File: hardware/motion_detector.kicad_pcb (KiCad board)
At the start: 2 copper layers, 45 x 25 mm, 36 parts, among them J1 Debug, P1 CON-SENSOR2, P2 Boot, U1 XMC1XXX24, U2 MCP4018, U3 AM612, U4 DRILL, U5 DRILL, U6 DRILL, U7 DRILL

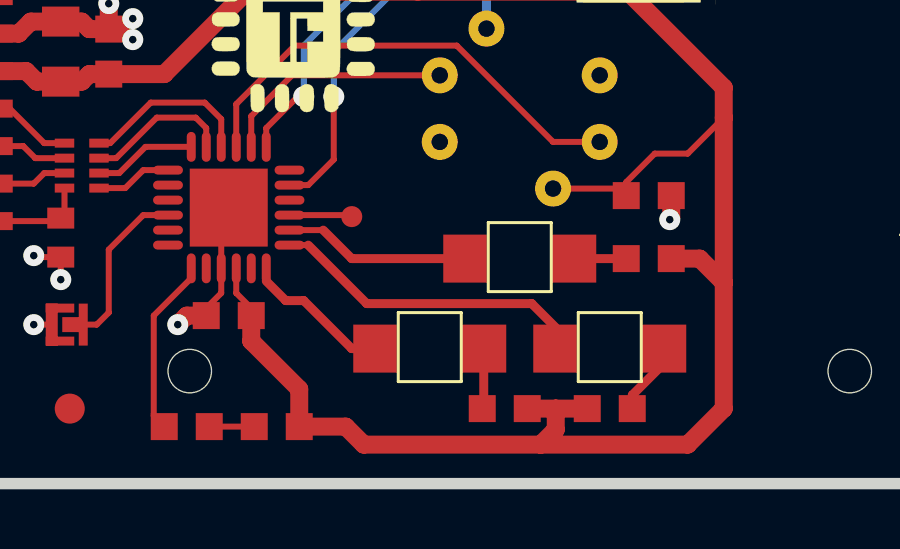
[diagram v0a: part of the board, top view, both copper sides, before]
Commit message: add cutouts for leds
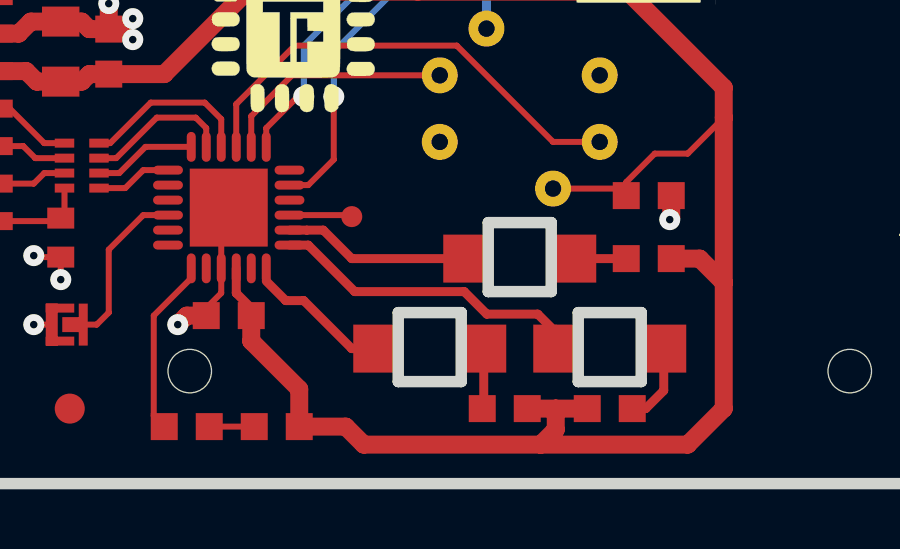
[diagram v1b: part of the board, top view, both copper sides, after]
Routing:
- net Net-(D3-Pad1): track 2.43 -> 3.20 mm
- net LED_GREEN: track 10.7 -> 11.3 mm
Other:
- outline, holes or cut-outs redrawn
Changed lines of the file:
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@@
     (area 42.044999 28.944999 282.27147 165.489573)
     (thickness 1.6002)
-    (drawings 13)
-    (tracks 211)
+    (drawings 25)
+    (tracks 216)
     (zones 0)
     (modules 36)
@@
   )
   (layers
-    (0 Vorderseite jumper hide)
+    (0 Vorderseite jumper)
     (31 Rückseite jumper hide)
     (32 B.Adhes user)
@@
     (34 B.Paste user)
     (35 F.Paste user)
-    (36 B.SilkS user)
-    (37 F.SilkS user hide)
+    (36 B.SilkS user hide)
+    (37 F.SilkS user)
     (38 B.Mask user)
     (39 F.Mask user)
@@
     (aux_axis_origin 42.9 54.8)
     (grid_origin 42.9 54.8)
-    (visible_elements FFFFBFBF)
+    (visible_elements FFFFDFBF)
     (pcbplotparams
       (layerselection 0x00030_80000001)
@@
       (xy 3.1242 -3.1242)) (layer B.SilkS) (width 0.00254))
   )
+  (gr_line (start 69.45 49.1) (end 67.35 49.1) (angle 90) (layer Edge.Cuts) (width 0.381))
+  (gr_line (start 69.45 51.4) (end 69.45 49.1) (angle 90) (layer Edge.Cuts) (width 0.381))
+  (gr_line (start 67.35 51.4) (end 69.45 51.4) (angle 90) (layer Edge.Cuts) (width 0.381))
+  (gr_line (start 67.35 49.1) (end 67.35 51.4) (angle 90) (layer Edge.Cuts) (width 0.381))
+  (gr_line (start 63.45 49.1) (end 61.35 49.1) (angle 90) (layer Edge.Cuts) (width 0.381))
+  (gr_line (start 63.45 51.4) (end 63.45 49.1) (angle 90) (layer Edge.Cuts) (width 0.381))
+  (gr_line (start 61.35 51.4) (end 63.45 51.4) (angle 90) (layer Edge.Cuts) (width 0.381))
+  (gr_line (start 61.35 49.1) (end 61.35 51.4) (angle 90) (layer Edge.Cuts) (width 0.381))
+  (gr_line (start 64.35 48.4) (end 64.35 46.1) (angle 90) (layer Edge.Cuts) (width 0.381))
+  (gr_line (start 66.45 48.4) (end 64.35 48.4) (angle 90) (layer Edge.Cuts) (width 0.381))
+  (gr_line (start 66.45 46.1) (end 66.45 48.4) (angle 90) (layer Edge.Cuts) (width 0.381))
+  (gr_line (start 64.35 46.1) (end 66.45 46.1) (angle 90) (layer Edge.Cuts) (width 0.381))
   (gr_text "Motion\nDetector\n2.0" (at 48.2 42.3) (layer B.SilkS)
     (effects (font (size 0.8 0.8) (thickness 0.15)) (justify mirror))
@@
   (segment (start 63.45 33.15) (end 63.45 31.7) (width 0.29972) (layer Vorderseite) (net 2))
   (segment (start 63.45 31.7) (end 63.55 31.6) (width 0.2) (layer Vorderseite) (net 2))
-  (segment (start 55.95 47.625) (end 55.95 48.45) (width 0.2) (layer Vorderseite) (net 2))
-  (segment (start 55.95 48.45) (end 56.45 48.95) (width 0.2) (layer Vorderseite) (net 2))
+  (segment (start 55.95 47.625) (end 55.95 48.45) (width 0.29972) (layer Vorderseite) (net 2))
+  (segment (start 55.95 48.45) (end 56.45 48.95) (width 0.29972) (layer Vorderseite) (net 2))
   (segment (start 56.45 48.95) (end 56.45 49.2) (width 0.2) (layer Vorderseite) (net 2))
   (segment (start 50.225 44.9493) (end 50.225 45.825) (width 0.2) (layer Vorderseite) (net 3))
@@
   (segment (start 55.05 52.9) (end 56.55 52.9) (width 0.2) (layer Vorderseite) (net 5))
   (segment (start 67.2 47.3) (end 68.95 47.3) (width 0.29972) (layer Vorderseite) (net 6))
-  (segment (start 57.725 46.35) (end 58.85 46.35) (width 0.2) (layer Vorderseite) (net 7))
-  (segment (start 59.8 47.3) (end 63.6 47.3) (width 0.29972) (layer Vorderseite) (net 7))
+  (segment (start 58.3 46.35) (end 57.725 46.35) (width 0.29972) (layer Vorderseite) (net 7))
   (segment (start 58.85 46.35) (end 59.8 47.3) (width 0.29972) (layer Vorderseite) (net 7))
+  (segment (start 59.8 47.3) (end 63.6 47.3) (width 0.29972) (layer Vorderseite) (net 7))
+  (segment (start 58.85 46.35) (end 58.3 46.35) (width 0.29972) (layer Vorderseite) (net 7))
+  (segment (start 70.2 50.3) (end 70.2 51.7) (width 0.29972) (layer Vorderseite) (net 8))
+  (segment (start 70.2 51.7) (end 69.6 52.3) (width 0.29972) (layer Vorderseite) (net 8))
+  (segment (start 69.6 52.3) (end 69.15 52.3) (width 0.29972) (layer Vorderseite) (net 8))
   (segment (start 70.2 50.3) (end 70.2 50.8) (width 0.29972) (layer Vorderseite) (net 8))
-  (segment (start 70.2 50.8) (end 69.15 51.85) (width 0.29972) (layer Vorderseite) (net 8))
-  (segment (start 69.15 51.85) (end 69.15 52.3) (width 0.29972) (layer Vorderseite) (net 8))
-  (segment (start 57.725 46.85) (end 58.35 46.85) (width 0.2) (layer Vorderseite) (net 9))
-  (segment (start 65.8 48.8) (end 66.6 49.6) (width 0.29972) (layer Vorderseite) (net 9))
-  (segment (start 60.3 48.8) (end 65.8 48.8) (width 0.29972) (layer Vorderseite) (net 9))
-  (segment (start 58.35 46.85) (end 60.3 48.8) (width 0.29972) (layer Vorderseite) (net 9))
+  (segment (start 58.35 46.85) (end 57.725 46.85) (width 0.29972) (layer Vorderseite) (net 9))
+  (segment (start 66.6 50.3) (end 66.6 49.75) (width 0.29972) (layer Vorderseite) (net 9))
+  (segment (start 66.6 49.75) (end 66 49.15) (width 0.29972) (layer Vorderseite) (net 9))
+  (segment (start 59.9 48.4) (end 58.35 46.85) (width 0.29972) (layer Vorderseite) (net 9))
+  (segment (start 63.55 48.4) (end 59.9 48.4) (width 0.29972) (layer Vorderseite) (net 9))
+  (segment (start 64.3 49.15) (end 63.55 48.4) (width 0.29972) (layer Vorderseite) (net 9))
+  (segment (start 66 49.15) (end 64.3 49.15) (width 0.29972) (layer Vorderseite) (net 9))
   (segment (start 66.6 49.6) (end 66.6 50.3) (width 0.2) (layer Vorderseite) (net 9))
   (segment (start 64.2 50.3) (end 64.2 52.25) (width 0.29972) (layer Vorderseite) (net 10))

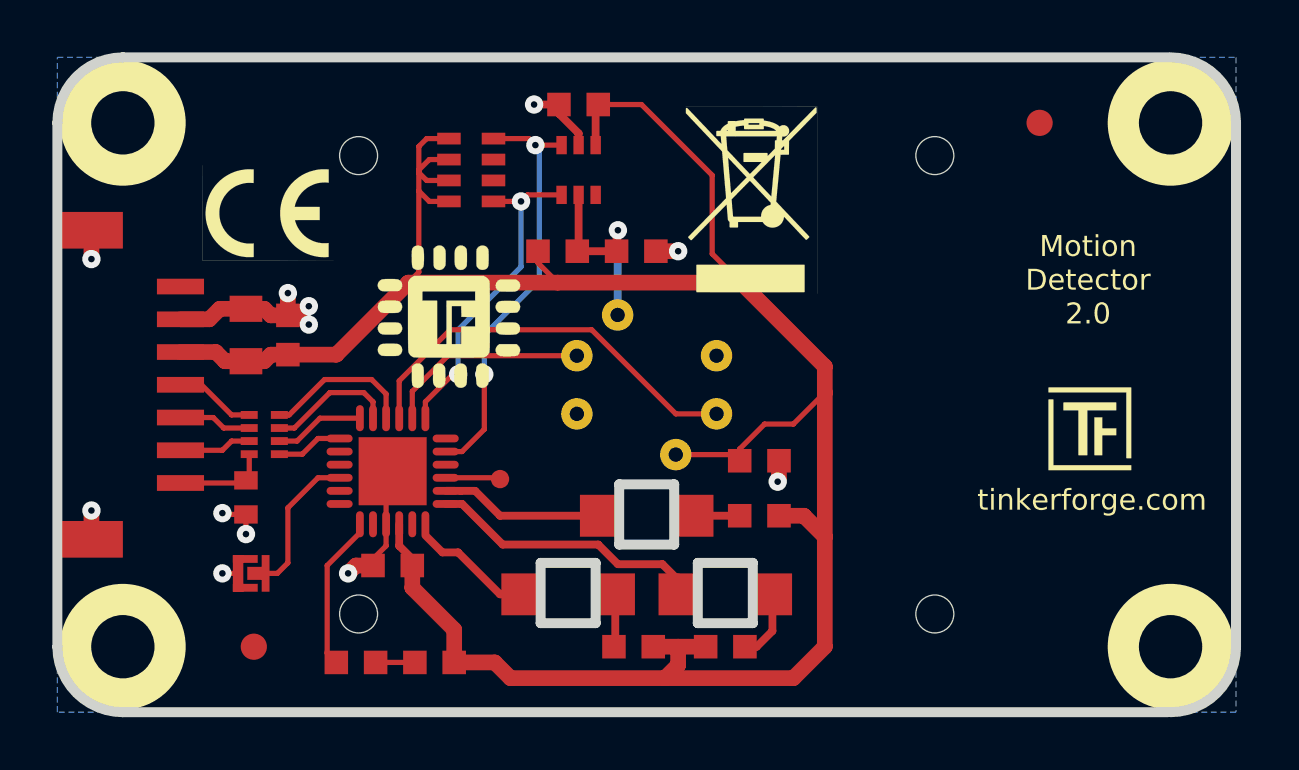
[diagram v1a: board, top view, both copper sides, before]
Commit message: fix ams612 routing, change led positions
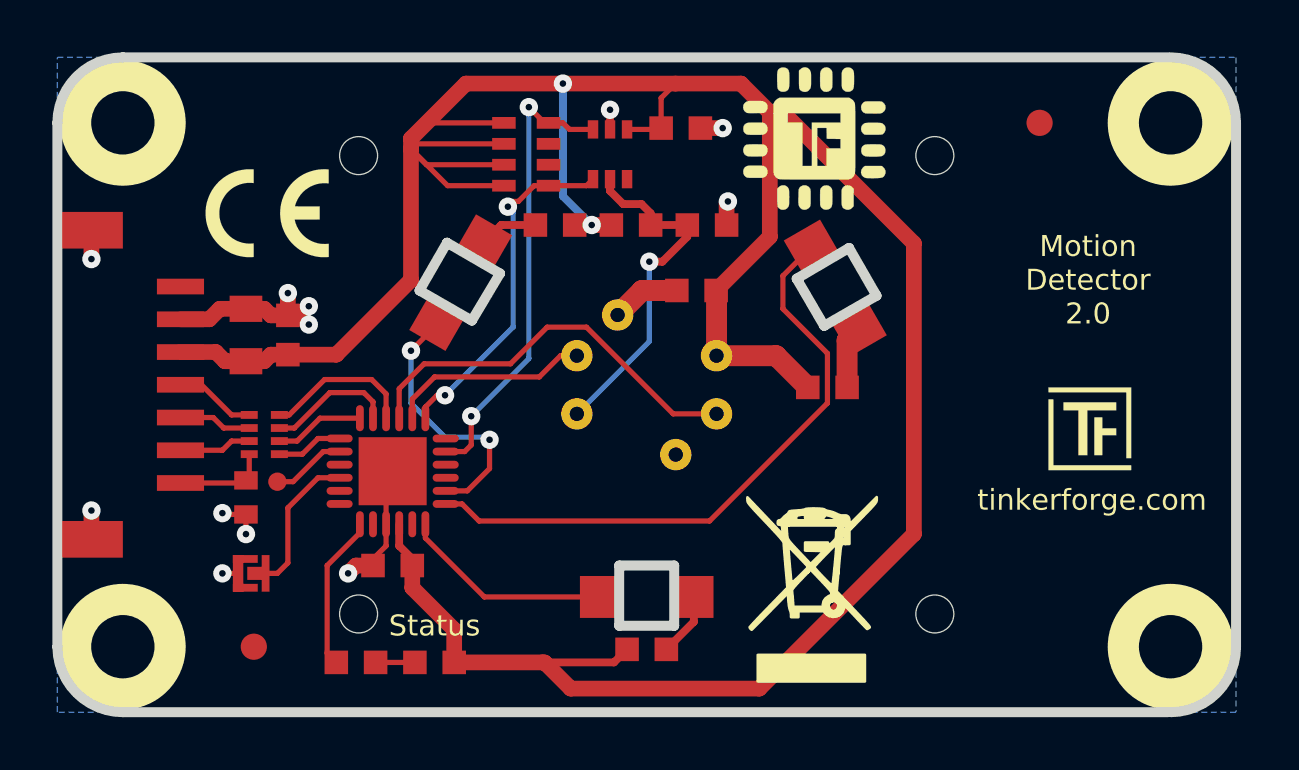
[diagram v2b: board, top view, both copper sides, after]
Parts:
- U4, U5, U6, U7: footprint kicad-libraries:DRILL_NP -> DRILL_NP
- VAL: footprint WEEE_7mm -> kicad-libraries:WEEE_7mm
- VAL: footprint CE_5mm -> kicad-libraries:CE_5mm
- moved G*** 15.5 mm to (71.8, 32.9)
- moved VAL 15.0 mm to (71.7, 50.1), turned to 0 degrees
- moved R3 13.6 mm to (61.9, 36.2)
- moved D3 12.4 mm to (72.6, 38.6), turned to 120 degrees
- moved D2 11.4 mm to (58.3, 38.4), turned to 240 degrees
- moved R4 10.6 mm to (72.3, 42.4)
- moved J1 8.50 mm to (51.3, 46.0)
- moved C7 6.93 mm to (67.3, 38.7), turned to 0 degrees
- moved C6 4.00 mm to (66.7, 32.5), turned to 180 degrees
- moved D4 3.00 mm to (65.4, 50.4)
- moved R2 2.97 mm to (64.8, 36.2)
- moved C5 2.88 mm to (67.7, 36.2)
- moved RP2 2.18 mm to (60.8, 33.5)
- moved U2 1.34 mm to (64.0, 33.5)
- moved R5 0.51 mm to (65.4, 52.4), turned to 180 degrees
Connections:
- U1 pad 15: Net-(J1-Pad1) -> (no net)
- U1 pad 2: (no net) -> Net-(J1-Pad1)
- U3 pad 1: GND -> VSENS
- U3 pad 3: VSENS -> GND
- U3 pad 4: GND -> VCC
- U3 pad 6: VCC -> GND
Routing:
- net VCC: track 95.4 -> 119.3 mm, vias 0 -> 2
- net LED_GREEN: track 11.3 -> 23.8 mm
- net VSENS: track 7.79 -> 13.7 mm
- net LED_RED: track 6.27 -> 10.2 mm, vias 0 -> 2
- net LED_BLUE: track 5.01 -> 8.53 mm
- net SCL: track 16.3 -> 17.7 mm
- net SDA: track 12.6 -> 13.4 mm
- net Net-(D3-Pad1): track 3.20 -> 2.43 mm
- net Net-(J1-Pad1): track 2.10 -> 2.85 mm
- net GND: track 25.6 -> 26.3 mm
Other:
- outline, holes or cut-outs redrawn
- board text added: "Status"

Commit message: version without i2c poti, uses rc circuit
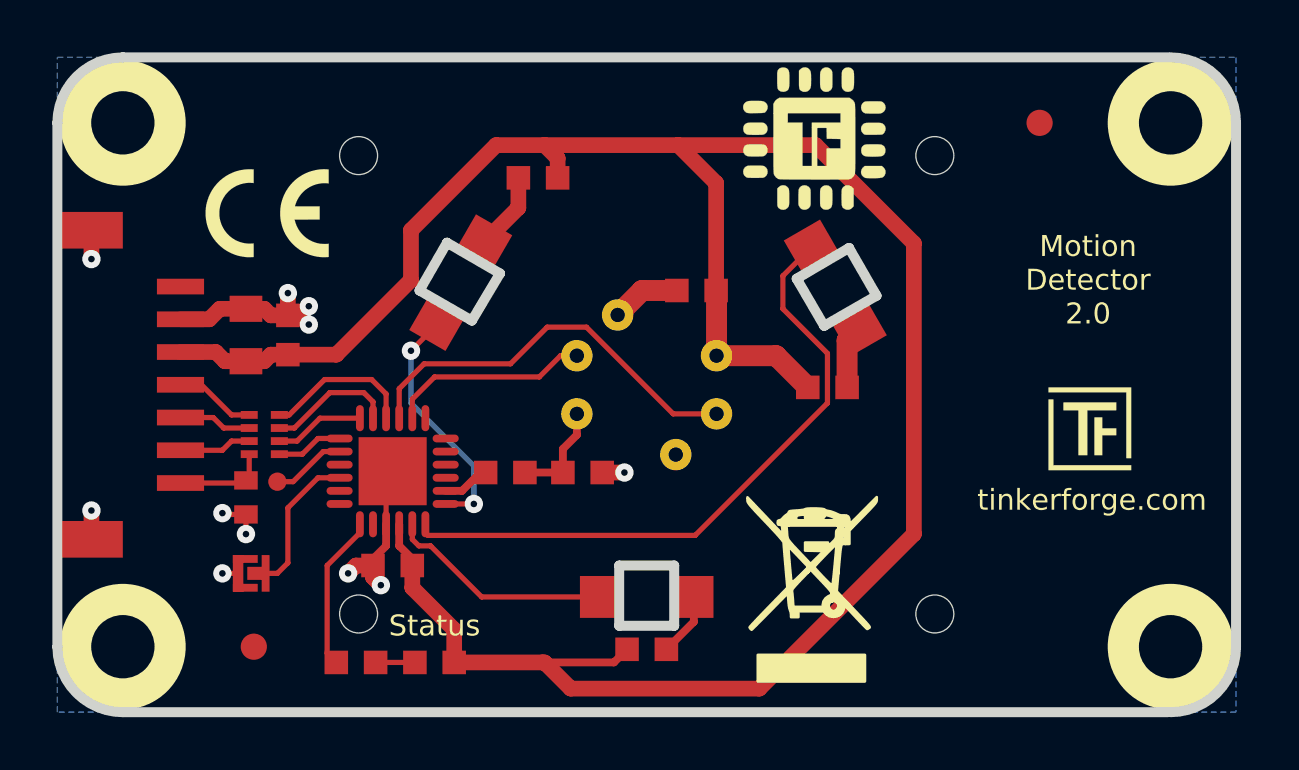
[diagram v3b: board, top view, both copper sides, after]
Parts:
- removed C5: 100nF, C0603F
- removed RP2: 4k7, kicad-libraries:4X0603
- removed U2: MCP4018, kicad-libraries:SC70-6
- R2: value 30k -> 1k
- moved C6 13.7 mm to (63.0, 45.6)
- moved R2 10.6 mm to (60.0, 45.6)
- moved R3 1.91 mm to (61.2, 34.4)
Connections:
- C6 pad 2: VCC -> VSENS
- R2 pad 1: VCC -> Net-(R2-Pad1)
- U1 pad 11: (no net) -> LED_BLUE
- U1 pad 12: LED_BLUE -> LED_GREEN
- U1 pad 13: LED_GREEN -> LED_RED
- U1 pad 14: LED_RED -> Net-(R2-Pad1)
- U1 pad 17: SCL -> (no net)
- U1 pad 19: SDA -> (no net)
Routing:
- net VCC: track 119.3 -> 89.4 mm, vias 2 -> 0
- net SCL: track 17.7 -> 0.00 mm, vias 2 -> 0
- net SDA: track 13.4 -> 0.00 mm, vias 2 -> 0
- net VSENS: track 13.7 -> 3.91 mm, vias 1 -> 0
- net Net-(R2-Pad1): track 0.00 -> 1.81 mm
- net LED_GREEN: track 23.8 -> 24.9 mm
- net GND: track 26.3 -> 25.5 mm, vias 12 -> 11
- net LED_RED: track 10.2 -> 9.37 mm
- net Net-(D2-Pad1): track 2.22 -> 2.98 mm

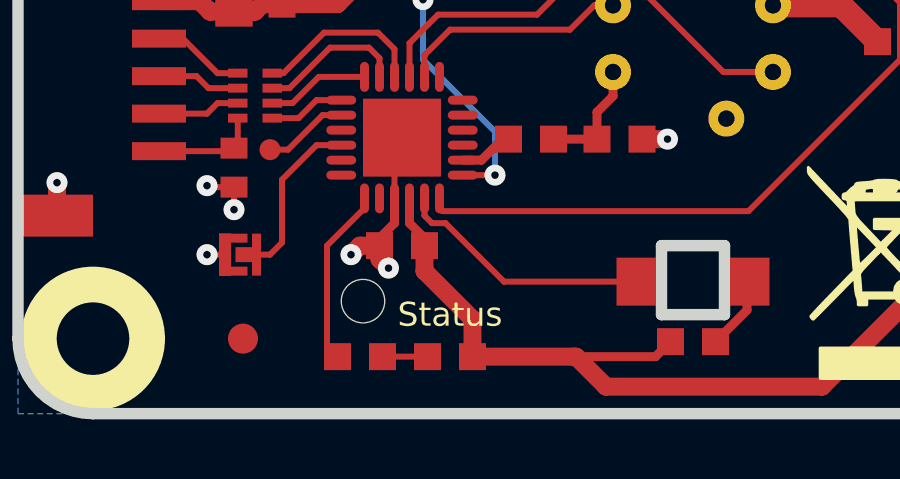
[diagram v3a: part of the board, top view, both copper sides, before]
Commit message: fix status led text
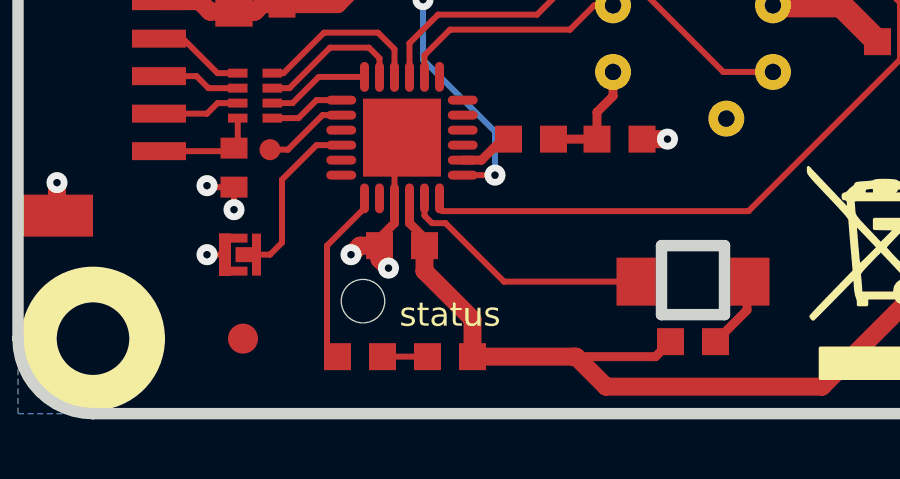
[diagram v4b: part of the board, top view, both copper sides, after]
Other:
- board text added: "status"
- board text removed: "Status"
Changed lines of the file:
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@@
     (links 53)
     (no_connects 0)
-    (area 42.709499 29.609499 88.090501 54.990501)
+    (area 42.044999 28.944999 282.27147 165.489573)
     (thickness 1.6002)
     (drawings 26)
@@
   )
   (layers
-    (0 Vorderseite jumper)
-    (31 Rückseite jumper)
+    (0 Vorderseite jumper hide)
+    (31 Rückseite jumper hide)
     (32 B.Adhes user)
     (33 F.Adhes user)
@@
   (gr_line (start 73.125 37.075) (end 74.175 38.9) (angle 90) (layer Edge.Cuts) (width 0.381))
   (gr_line (start 71.125 38.25) (end 73.125 37.075) (angle 90) (layer Edge.Cuts) (width 0.381))
-  (gr_text Status (at 57.3 51.5) (layer F.SilkS)
+  (gr_text status (at 57.3 51.5) (layer F.SilkS)
     (effects (font (size 0.8 0.8) (thickness 0.15)))
   )

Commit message: change rgb leds to 3x blue
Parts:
- D2: value red_inv -> blue_inv
- D3: value green_inv -> blue_inv
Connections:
- net LED_BLUE renamed LED_BTM
- net LED_GREEN renamed LED_TOP_R
- net LED_RED renamed LED_TOP_L

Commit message: specify prozessor type
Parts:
- U1: value XMC1XXX24 -> XMC110024
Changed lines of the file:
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@@
     (links 53)
     (no_connects 0)
-    (area 42.709499 29.609499 88.090501 54.990501)
+    (area 42.044999 28.944999 282.27147 165.489573)
     (thickness 1.6002)
     (drawings 26)
@@
   )
   (layers
-    (0 Vorderseite jumper hide)
-    (31 Rückseite jumper hide)
+    (0 Vorderseite jumper)
+    (31 Rückseite jumper)
     (32 B.Adhes user)
     (33 F.Adhes user)
@@
     (aux_axis_origin 42.9 54.8)
     (grid_origin 42.9 54.8)
-    (visible_elements FFFF5F9F)
+    (visible_elements FFFF5FFF)
     (pcbplotparams
       (layerselection 0x00030_80000001)
@@
       (effects (font (size 0.3 0.3) (thickness 0.075)))
     )
-    (fp_text value XMC1XXX24 (at 0 0.8) (layer F.Fab)
+    (fp_text value XMC110024 (at 0 0.8) (layer F.Fab)
       (effects (font (size 0.3 0.3) (thickness 0.075)))
     )
